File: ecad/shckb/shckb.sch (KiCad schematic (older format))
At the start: 30 parts, among them SW1 SW_Keyboard, SW10 SW_Keyboard, SW11 SW_Keyboard, SW12 SW_Keyboard, SW13 SW_Keyboard, SW14 SW_Keyboard, SW15 SW_Keyboard, SW16 SW_Keyboard, SW17 SW_Keyboard, SW18 SW_Keyboard, SW19 SW_Keyboard, SW2 SW_Keyboard, SW20 SW_Keyboard, SW21 SW_Keyboard, SW22 SW_Keyboard, SW23 SW_Keyboard, SW24 SW_Keyboard, SW25 SW_Keyboard, SW26 SW_Keyboard, SW27 SW_Keyboard, SW28 SW_Keyboard, SW29 SW_Keyboard, SW3 SW_Keyboard, SW30 SW_Keyboard, SW4 SW_Keyboard, SW5 SW_Keyboard, SW6 SW_Keyboard, SW7 SW_Keyboard, SW8 SW_Keyboard, SW9 SW_Keyboard

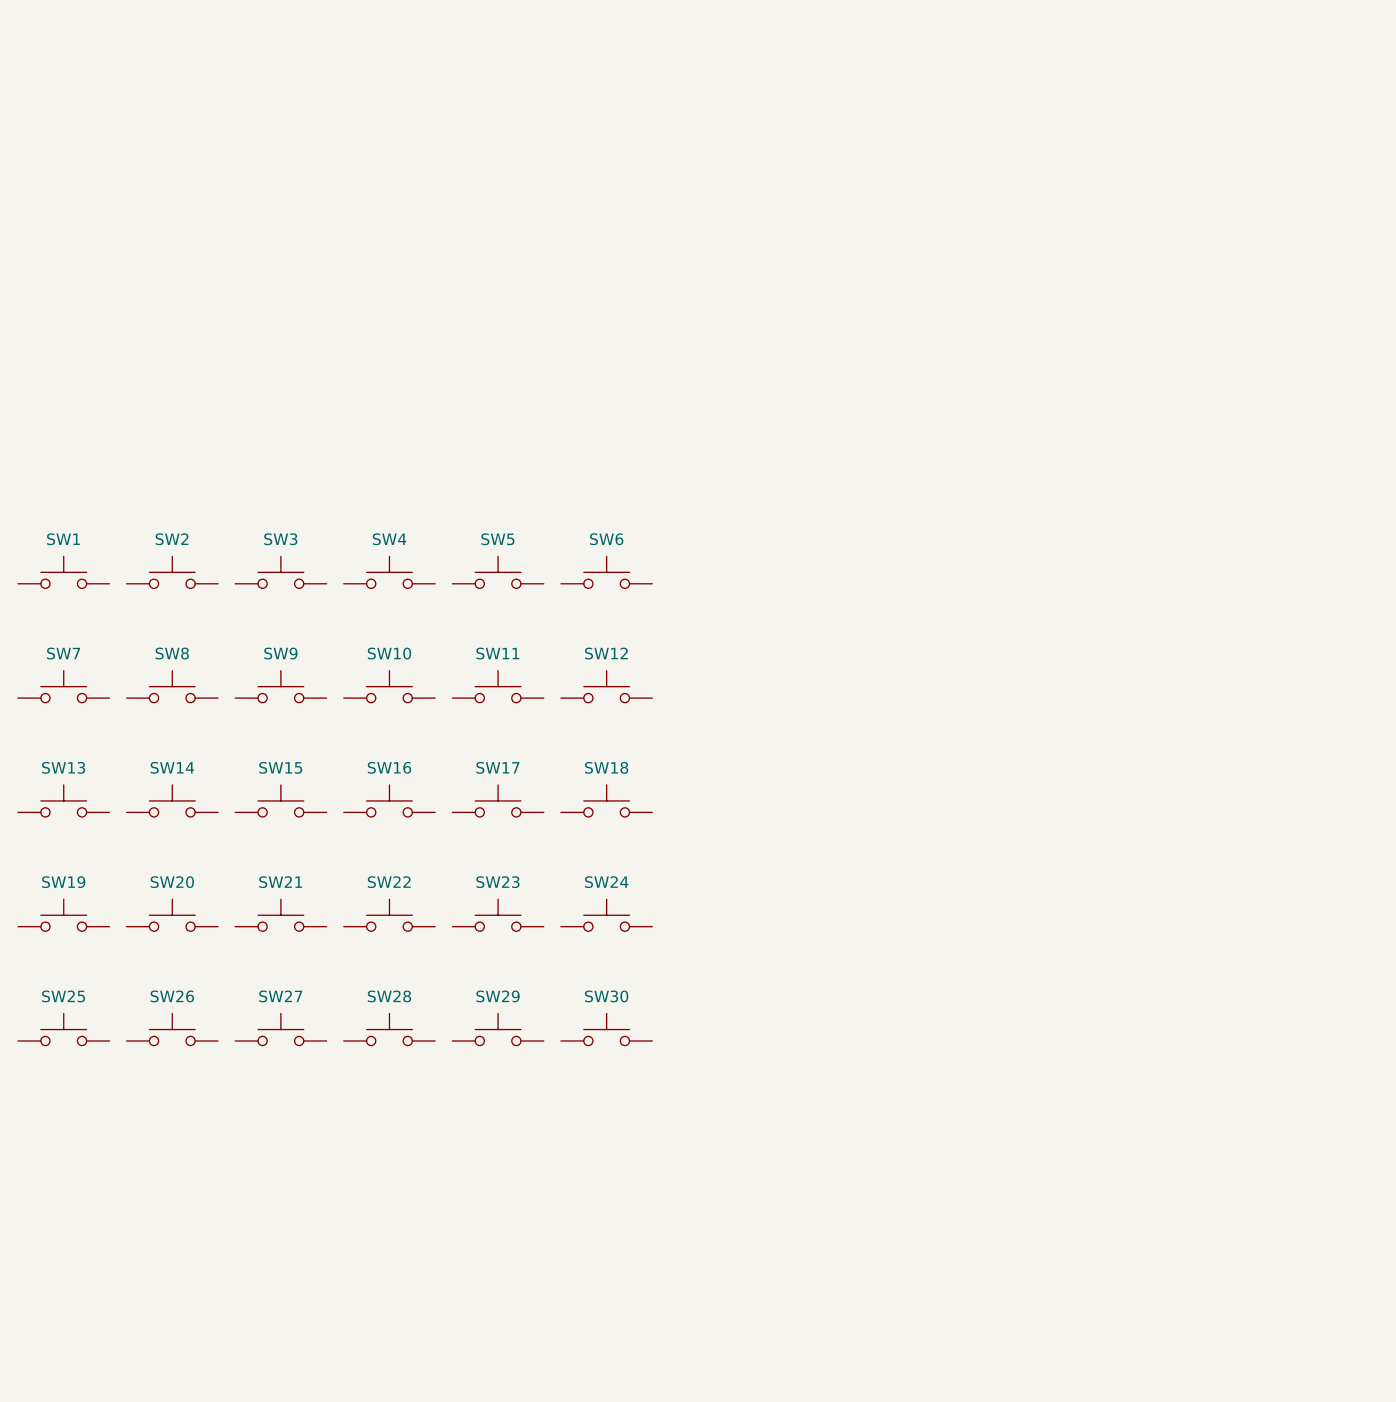
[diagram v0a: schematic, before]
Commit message: created the keyboard matrix in the schematic
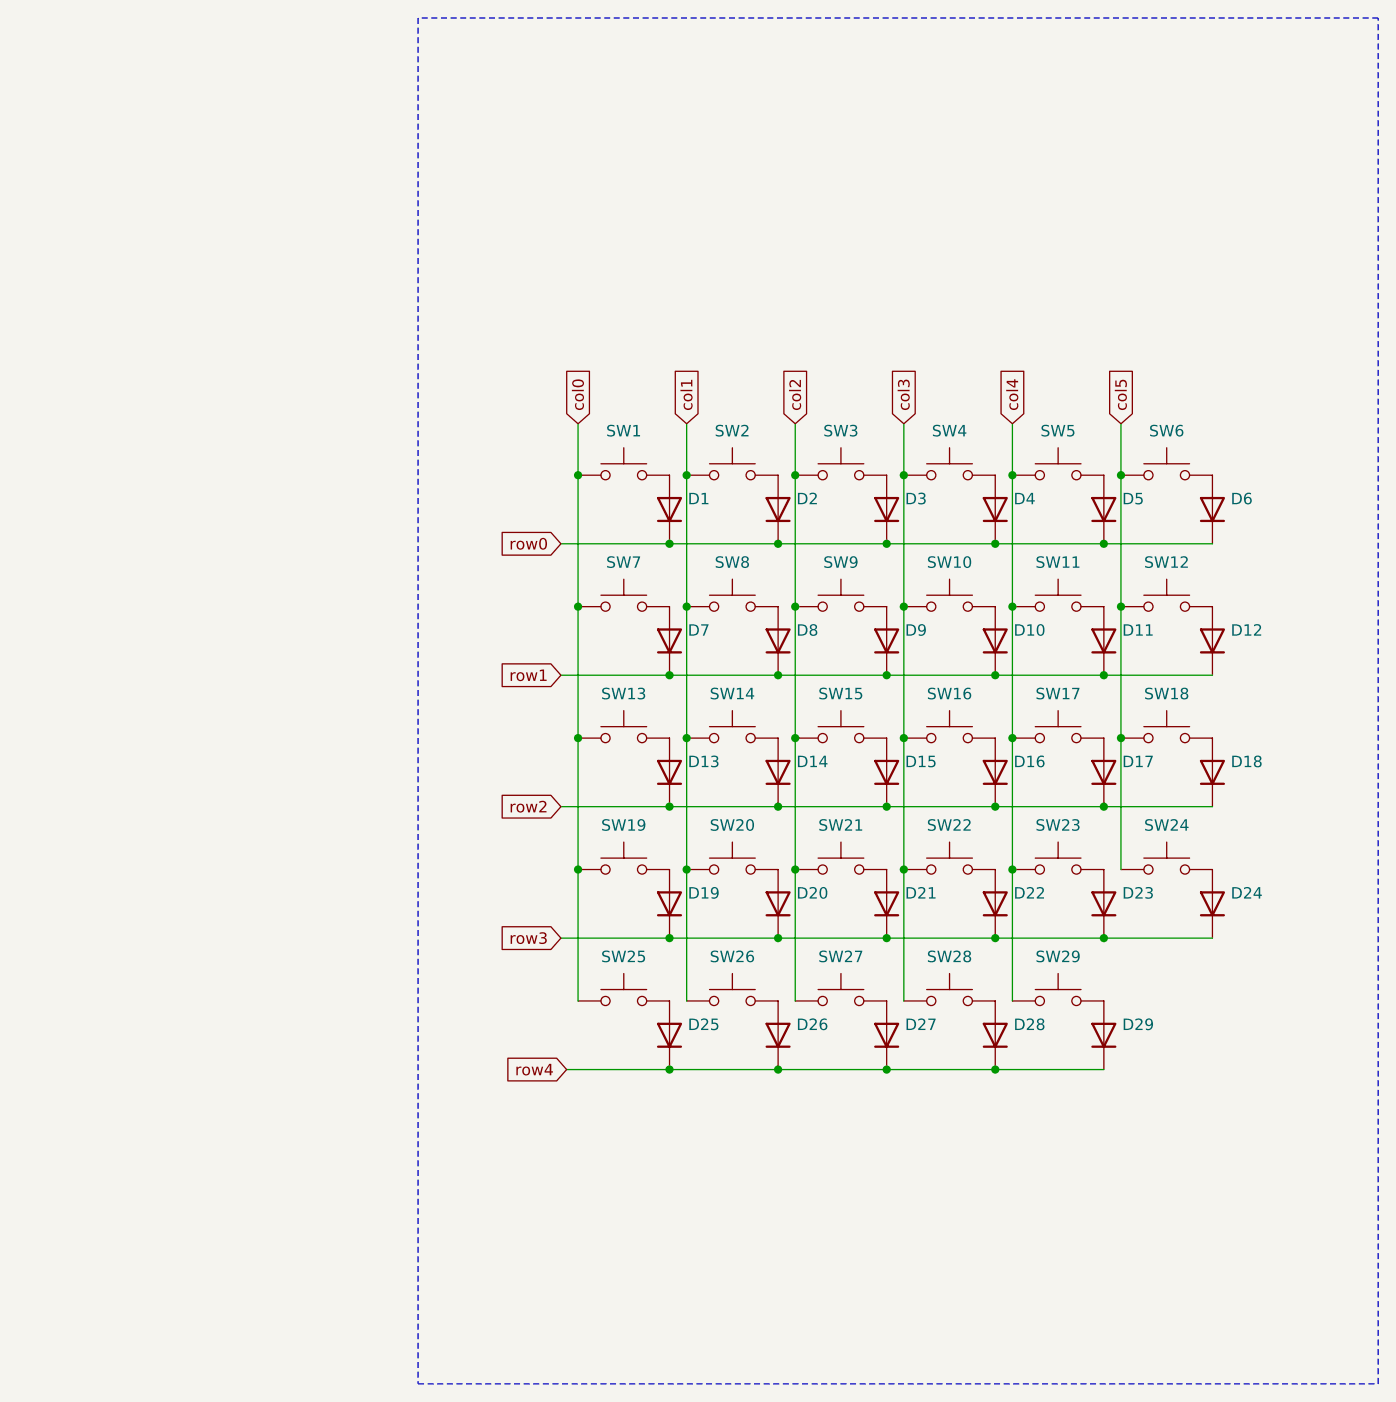
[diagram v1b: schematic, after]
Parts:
- removed SW30: SW_Keyboard, symbol shckb:SW_Keyboard
- added D1, D10, D11, D12, D13, D14, D15, D16, D17, D18, D19, D2, D20, D21, D22, D23, D24, D25, D26, D27, D28, D29, D3, D4, D5, D6, D7, D8, D9: D, symbol shckb:D
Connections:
- net col1: now reaches SW2.1
- net col1: now also SW14.1, SW20.1, SW26.1, SW8.1
- net at SW2.2: now also D2.2 (A)
- net col2: now reaches SW3.1
- net col2: now also SW15.1, SW21.1, SW27.1, SW9.1
- net at SW3.2: now also D3.2 (A)
- net col3: now reaches SW4.1
- net col3: now also SW10.1, SW16.1, SW22.1, SW28.1
- net at SW4.2: now also D4.2 (A)
- net col4: now reaches SW5.1
- net col4: now also SW11.1, SW17.1, SW23.1, SW29.1
- net at SW5.2: now also D5.2 (A)
- net col5: now reaches SW6.1
- net col5: now also SW12.1, SW18.1, SW24.1
- net at SW6.2: now also D6.2 (A)
- net col0: now reaches SW1.1
- net col0: now also SW13.1, SW19.1, SW25.1, SW7.1
- net at SW1.2: now also D1.2 (A)
- net at SW8.2: now also D8.2 (A)
- net at SW9.2: now also D9.2 (A)
- net at SW10.2: now also D10.2 (A)
- net at SW11.2: now also D11.2 (A)
- net at SW12.2: now also D12.2 (A)
- net at SW7.2: now also D7.2 (A)
- net at SW14.2: now also D14.2 (A)
- net at SW15.2: now also D15.2 (A)
- net at SW16.2: now also D16.2 (A)
- net at SW17.2: now also D17.2 (A)
- net at SW18.2: now also D18.2 (A)
- net at SW13.2: now also D13.2 (A)
- net at SW20.2: now also D20.2 (A)
- net at SW21.2: now also D21.2 (A)
- net at SW22.2: now also D22.2 (A)
- net at SW23.2: now also D23.2 (A)
- net at SW24.2: now also D24.2 (A)
- net at SW19.2: now also D19.2 (A)
- net at SW26.2: now also D26.2 (A)
- net at SW27.2: now also D27.2 (A)
- net at SW28.2: now also D28.2 (A)
- net at SW29.2: now also D29.2 (A)
- net at SW25.2: now also D25.2 (A)
- new net row0: D1.1 (K), D2.1 (K), D3.1 (K), D4.1 (K), D5.1 (K), D6.1 (K)
- new net row1: D10.1 (K), D11.1 (K), D12.1 (K), D7.1 (K), D8.1 (K), D9.1 (K)
- new net row2: D13.1 (K), D14.1 (K), D15.1 (K), D16.1 (K), D17.1 (K), D18.1 (K)
- new net row3: D19.1 (K), D20.1 (K), D21.1 (K), D22.1 (K), D23.1 (K), D24.1 (K)
- new net row4: D25.1 (K), D26.1 (K), D27.1 (K), D28.1 (K), D29.1 (K)
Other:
- moved on the sheet: SW1, SW10, SW11, SW12, SW13, SW14, SW15, SW16, SW17, SW18, SW19, SW2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
